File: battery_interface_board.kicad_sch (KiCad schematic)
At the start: 0 parts

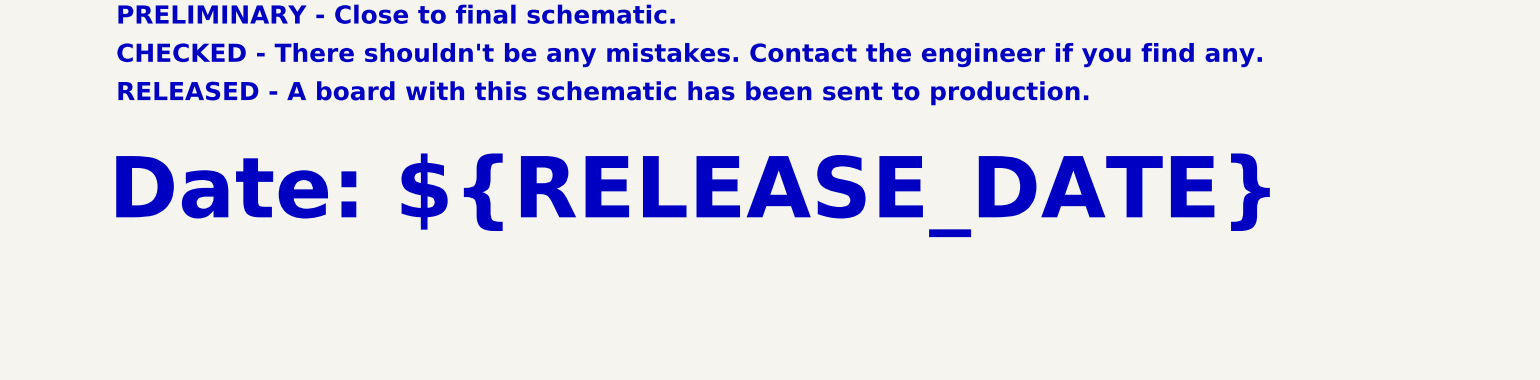
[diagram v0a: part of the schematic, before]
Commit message: SCH[Clean]: Cleaned up some schmatic errors.
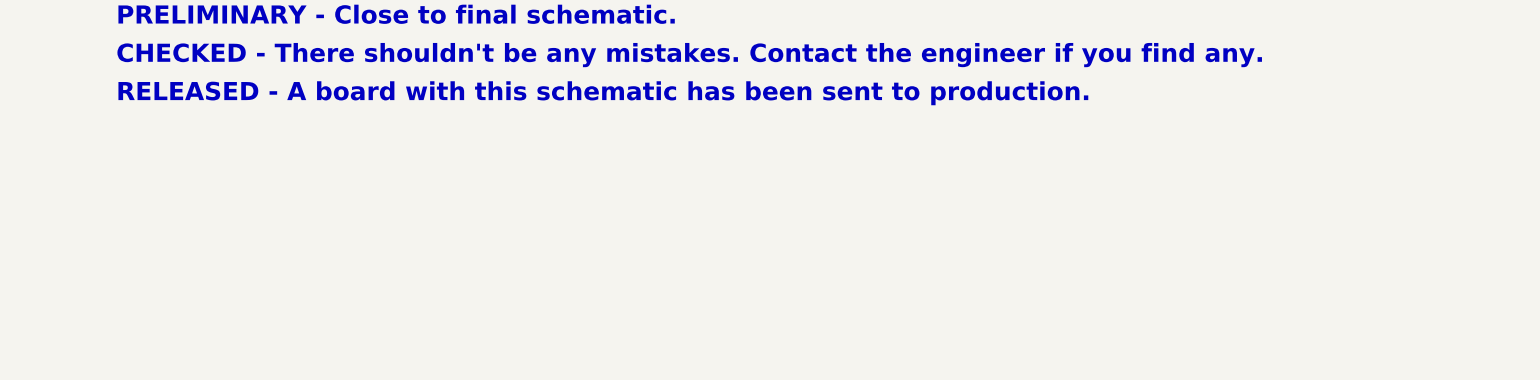
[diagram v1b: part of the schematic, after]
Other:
- note removed: "Date: ${RELEASE_DATE}"
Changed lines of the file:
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@@
-		)
-	)
-	(text "Date: ${RELEASE_DATE}"
-		(exclude_from_sim no)
-		(at 220.98 237.49 0)
-		(effects
-			(font
-				(face "Times New Roman")
-				(size 10.16 10.16)
-				(thickness 0.6)
-				(bold yes)
-				(color 200 200 200 1)
-			)
-			(justify left bottom)
 		)
 	)

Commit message: PCB[Connector, Clearnces]: Testing clearances.
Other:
- note added: "${PROJECT_NAME}"
- note removed: "${BOARD_NAME}"
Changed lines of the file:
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@@
 		)
 	)
-	(text "${BOARD_NAME}"
+	(text "${PROJECT_NAME}"
 		(exclude_from_sim no)
 		(at 25.4 40.64 0)
